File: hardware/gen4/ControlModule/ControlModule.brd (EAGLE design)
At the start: 29.9 x 59.3 mm, 39 parts, among them IC1 XMEGA16A4A

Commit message: pdi fix
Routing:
- net DATA: track 0.00 -> 37.0 mm, vias 0 -> 1
- net GND: track 111.1 -> 108.1 mm
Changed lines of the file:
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@@
 <wire x1="41.43375" y1="9.2075" x2="42.4815" y2="9.2075" width="0.254" layer="1"/>
 <wire x1="42.4815" y1="9.2075" x2="42.545" y2="9.271" width="0.254" layer="1"/>
-<wire x1="42.46" y1="26.06" x2="43.79" y2="26.06" width="0.1524" layer="1"/>
-<wire x1="43.79" y1="26.06" x2="45.24375" y2="24.685625" width="0.1524" layer="1"/>
-<wire x1="45.24375" y1="24.685625" x2="45.24375" y2="20.955" width="0.1524" layer="1"/>
+<wire x1="42.46" y1="26.06" x2="43.31375" y2="26.06" width="0.1524" layer="1"/>
+<wire x1="43.31375" y1="26.06" x2="45.24375" y2="24.28875" width="0.1524" layer="1"/>
+<wire x1="45.24375" y1="24.28875" x2="45.24375" y2="20.955" width="0.1524" layer="1"/>
 <wire x1="45.24375" y1="20.955" x2="44.45" y2="20.16125" width="0.1524" layer="1"/>
 <wire x1="44.45" y1="20.16125" x2="44.45" y2="19.3675" width="0.1524" layer="1"/>
@@
 <contactref element="S3" pad="2"/>
 <contactref element="S1" pad="2"/>
-<wire x1="61.595" y1="22.225" x2="59.84875" y2="22.225" width="0.254" layer="16"/>
-<wire x1="59.84875" y1="22.225" x2="58.7375" y2="21.11375" width="0.254" layer="16"/>
+<wire x1="58.42" y1="20.955" x2="58.57875" y2="20.955" width="0.254" layer="16"/>
+<wire x1="58.57875" y1="20.955" x2="58.7375" y2="21.11375" width="0.254" layer="16"/>
 <wire x1="58.7375" y1="21.11375" x2="58.7375" y2="20.32" width="0.254" layer="16"/>
 <wire x1="58.7375" y1="19.605625" x2="58.7375" y2="20.32" width="0.254" layer="16"/>
@@
 <wire x1="38.338125" y1="21.581875" x2="39.37" y2="20.55" width="0.1778" layer="1"/>
 <contactref element="JP2" pad="6"/>
+<wire x1="59.21375" y1="30.00375" x2="54.06" y2="23.66" width="0" layer="19" extent="1-1"/>
 </signal>
 <signal name="3.3V">
@@
 <wire x1="45.86" y1="27.1275" x2="45.085" y2="26.3525" width="0.254" layer="1"/>
 <wire x1="45.085" y1="26.3525" x2="44.1325" y2="26.3525" width="0.254" layer="1"/>
-<wire x1="44.1325" y1="26.3525" x2="43.65625" y2="26.82875" width="0.254" layer="1"/>
-<wire x1="43.65625" y1="26.82875" x2="43.65625" y2="27.305" width="0.254" layer="1"/>
+<wire x1="44.1325" y1="26.3525" x2="43.815" y2="26.749375" width="0.254" layer="1"/>
+<wire x1="43.815" y1="26.749375" x2="43.65625" y2="27.305" width="0.254" layer="1"/>
 <wire x1="43.65625" y1="27.305" x2="43.4975" y2="27.46375" width="0.254" layer="1"/>
 <wire x1="43.4975" y1="27.46375" x2="40.9575" y2="27.46375" width="0.254" layer="1"/>
@@
 <contactref element="IC1" pad="34"/>
 <contactref element="JP2" pad="1"/>
-<wire x1="42.46" y1="26.86" x2="60.325" y2="26.035" width="0" layer="19" extent="1-1"/>
+<wire x1="42.46" y1="26.86" x2="43.3075" y2="26.86" width="0.1778" layer="1"/>
+<wire x1="43.3075" y1="26.86" x2="43.33875" y2="26.82875" width="0.1778" layer="1"/>
+<wire x1="43.33875" y1="26.82875" x2="43.33875" y2="26.51125" width="0.1778" layer="1"/>
+<wire x1="43.33875" y1="26.51125" x2="44.60875" y2="25.24125" width="0.1778" layer="1"/>
+<wire x1="44.60875" y1="25.24125" x2="47.46625" y2="25.24125" width="0.1778" layer="1"/>
+<wire x1="47.46625" y1="25.24125" x2="48.021875" y2="24.685625" width="0.1778" layer="1"/>
+<wire x1="48.021875" y1="24.685625" x2="49.768125" y2="24.685625" width="0.1778" layer="1"/>
+<wire x1="49.768125" y1="24.685625" x2="50.244375" y2="24.209375" width="0.1778" layer="1"/>
+<wire x1="50.244375" y1="24.209375" x2="50.244375" y2="19.05" width="0.1778" layer="1"/>
+<via x="50.244375" y="19.05" extent="1-16" drill="0.6"/>
+<wire x1="50.244375" y1="19.05" x2="50.561875" y2="19.05" width="0.1778" layer="16"/>
+<wire x1="50.561875" y1="19.05" x2="51.038125" y2="19.52625" width="0.1778" layer="16"/>
+<wire x1="51.038125" y1="19.52625" x2="51.038125" y2="21.2725" width="0.1778" layer="16"/>
+<wire x1="51.038125" y1="21.2725" x2="51.355625" y2="21.59" width="0.1778" layer="16"/>
+<wire x1="51.355625" y1="21.59" x2="51.831875" y2="21.59" width="0.1778" layer="16"/>
+<wire x1="51.831875" y1="21.59" x2="52.22875" y2="21.193125" width="0.1778" layer="16"/>
+<wire x1="52.22875" y1="21.193125" x2="52.22875" y2="19.446875" width="0.1778" layer="16"/>
+<wire x1="52.22875" y1="19.446875" x2="53.18125" y2="18.494375" width="0.1778" layer="16"/>
+<wire x1="53.18125" y1="18.494375" x2="58.181875" y2="18.494375" width="0.1778" layer="16"/>
+<wire x1="58.181875" y1="18.494375" x2="59.3725" y2="19.685" width="0.1778" layer="16"/>
+<wire x1="59.3725" y1="19.685" x2="59.3725" y2="19.84375" width="0.1778" layer="16"/>
+<wire x1="59.3725" y1="19.84375" x2="59.293125" y2="20.79625" width="0.1778" layer="16"/>
+<wire x1="59.293125" y1="20.79625" x2="59.293125" y2="21.74875" width="0.1778" layer="16"/>
+<wire x1="59.293125" y1="21.74875" x2="59.769375" y2="22.225" width="0.1778" layer="16"/>
+<wire x1="59.769375" y1="22.225" x2="61.43625" y2="22.225" width="0.1778" layer="16"/>
+<wire x1="61.43625" y1="22.225" x2="61.595" y2="22.38375" width="0.1778" layer="16"/>
+<wire x1="61.595" y1="22.38375" x2="61.595" y2="24.765" width="0.1778" layer="16"/>
+<wire x1="61.595" y1="24.765" x2="60.325" y2="26.035" width="0.1778" layer="16"/>
 </signal>
 <signal name="SS_4">

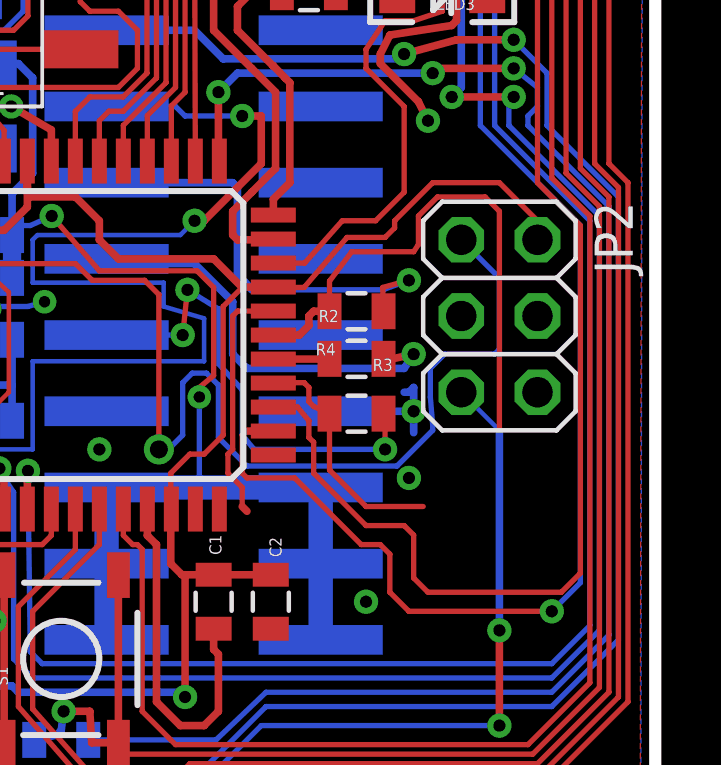
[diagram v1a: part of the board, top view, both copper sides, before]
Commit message: redid debug connector on comms, but clearance checks havent been done
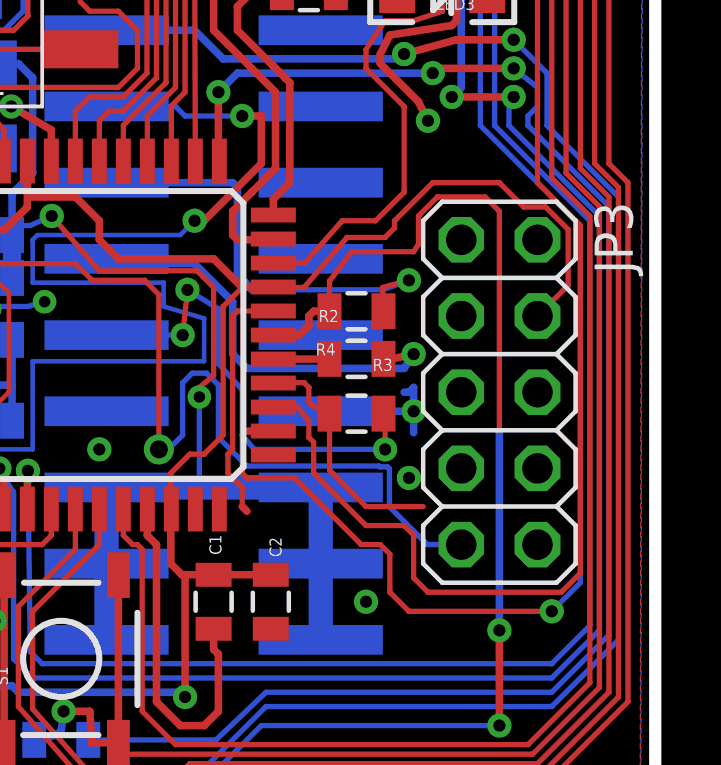
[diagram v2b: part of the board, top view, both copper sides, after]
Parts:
- removed JP2: (no value), pinhead:2X03
- added JP3: DEBUG, pinhead:2X05
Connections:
- net N$1 renamed AVCC
- removed net INT: IC1.12
- removed net SCL: IC1.11
- removed net SDA: IC1.10
- net 3.3V: now also JP3.4; no longer JP2.2
- net DATA: now also JP3.9; no longer JP2.1
- net GND: now also JP3.10; no longer JP2.6
- net RESET: now also JP3.6; no longer JP2.5
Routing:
- net DATA: track 37.0 -> 30.5 mm
- net 3.3V: track 163.0 -> 166.8 mm
- net RESET: track 58.1 -> 56.3 mm
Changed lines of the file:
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@@
 <?xml version="1.0" encoding="utf-8"?>
 <!DOCTYPE eagle SYSTEM "eagle.dtd">
-<eagle version="7.2.0">
+<eagle version="7.5.0">
 <drawing>
 <settings>
@@
 <setting verticaltext="up"/>
 </settings>
-<grid distance="25" unitdist="mil" unit="mil" style="lines" multiple="1" display="yes" altdistance="3.125" altunitdist="mil" altunit="mil"/>
+<grid distance="0.000123031496" unitdist="mil" unit="mil" style="lines" multiple="1" display="yes" altdistance="0.000123031496" altunitdist="mil" altunit="mil"/>
 <layers>
 <layer number="1" name="Top" color="4" fill="1" visible="yes" active="yes"/>
@@
 <attribute name="PROD_ID" value="SWCH-08247" x="46.99" y="12.065" size="1.778" layer="27" rot="R90" display="off"/>
 </element>
-<element name="JP2" library="pinhead" package="2X03" value="" x="61.595" y="23.495" rot="R270"/>
+<element name="JP3" library="pinhead" package="2X05" value="DEBUG" x="61.595" y="20.955" rot="R270"/>
 </elements>
 <signals>
@@
 <wire x1="51.435" y1="7.62" x2="40.64" y2="7.62" width="0.1778" layer="16"/>
 <wire x1="40.64" y1="7.62" x2="40.005" y2="8.255" width="0.1778" layer="16"/>
-<contactref element="JP2" pad="5"/>
-<wire x1="61.595" y1="19.685" x2="60.325" y2="20.955" width="0.1524" layer="16"/>
+<contactref element="JP3" pad="6"/>
+<wire x1="61.595" y1="19.685" x2="62.865" y2="20.955" width="0" layer="19" extent="16-16"/>
 </signal>
 <signal name="GND">
@@
 <wire x1="38.338125" y1="24.844375" x2="38.338125" y2="21.581875" width="0.1778" layer="1"/>
 <wire x1="38.338125" y1="21.581875" x2="39.37" y2="20.55" width="0.1778" layer="1"/>
-<contactref element="JP2" pad="6"/>
-<wire x1="59.21375" y1="30.00375" x2="54.06" y2="23.66" width="0" layer="19" extent="1-1"/>
+<contactref element="JP3" pad="10"/>
+<wire x1="55.6387" y1="20.32" x2="52.705" y2="19.05" width="0" layer="19" extent="1-16"/>
 </signal>
 <signal name="3.3V">
@@
 <wire x1="40.9575" y1="27.46375" x2="40.64" y2="27.78125" width="0.254" layer="1"/>
 <via x="40.64" y="27.78125" extent="1-16" drill="0.4064" diameter="0.254"/>
-<wire x1="62.865" y1="26.67" x2="61.595" y2="27.94" width="0.1778" layer="1"/>
 <wire x1="61.595" y1="27.94" x2="59.3725" y2="27.94" width="0.1778" layer="1"/>
 <wire x1="59.3725" y1="27.94" x2="58.1025" y2="26.67" width="0.1778" layer="1"/>
@@
 <wire x1="38.1" y1="34.925" x2="39.575" y2="34.925" width="0.1524" layer="16"/>
 <wire x1="39.575" y1="34.925" x2="39.61" y2="34.89" width="0.254" layer="16"/>
-<contactref element="JP2" pad="2"/>
-<wire x1="62.865" y1="26.67" x2="62.865" y2="26.035" width="0.1524" layer="1"/>
+<contactref element="JP3" pad="4"/>
+<wire x1="61.595" y1="27.94" x2="62.40429375" y2="27.13070625" width="0.1778" layer="1"/>
+<wire x1="62.40429375" y1="27.13070625" x2="63.135603125" y2="27.13070625" width="0.1778" layer="1"/>
+<wire x1="63.135603125" y1="27.13070625" x2="63.88685" y2="26.379459375" width="0.1778" layer="1"/>
+<wire x1="63.88685" y1="26.379459375" x2="63.88685" y2="24.51685" width="0.1778" layer="1"/>
+<wire x1="63.88685" y1="24.51685" x2="62.865" y2="23.495" width="0.1778" layer="1"/>
 </signal>
-<signal name="N$1">
+<signal name="AVCC">
 <contactref element="IC1" pad="39"/>
 <contactref element="R1" pad="1"/>
@@
 <wire x1="46.99" y1="9.68375" x2="47.069375" y2="10.31875" width="0.254" layer="16"/>
 </signal>
-<signal name="SCL">
-<contactref element="IC1" pad="11"/>
-</signal>
-<signal name="SDA">
-<contactref element="IC1" pad="10"/>
-</signal>
 <signal name="12V">
 <contactref element="R8" pad="2"/>
@@
 <wire x1="58.42" y1="43.18" x2="55.6387" y2="43.18" width="0.254" layer="16"/>
 </signal>
-<signal name="INT">
-<contactref element="IC1" pad="12"/>
-</signal>
 <signal name="GLED1">
 <contactref element="R13" pad="2"/>
@@
 <signal name="DATA">
 <contactref element="IC1" pad="34"/>
-<contactref element="JP2" pad="1"/>
 <wire x1="42.46" y1="26.86" x2="43.3075" y2="26.86" width="0.1778" layer="1"/>
 <wire x1="43.3075" y1="26.86" x2="43.33875" y2="26.82875" width="0.1778" layer="1"/>
@@
 <wire x1="52.22875" y1="21.193125" x2="52.22875" y2="19.446875" width="0.1778" layer="16"/>
 <wire x1="52.22875" y1="19.446875" x2="53.18125" y2="18.494375" width="0.1778" layer="16"/>
-<wire x1="53.18125" y1="18.494375" x2="58.181875" y2="18.494375" width="0.1778" layer="16"/>
-<wire x1="58.181875" y1="18.494375" x2="59.3725" y2="19.685" width="0.1778" layer="16"/>
-<wire x1="59.3725" y1="19.685" x2="59.3725" y2="19.84375" width="0.1778" layer="16"/>
-<wire x1="59.3725" y1="19.84375" x2="59.293125" y2="20.79625" width="0.1778" layer="16"/>
-<wire x1="59.293125" y1="20.79625" x2="59.293125" y2="21.74875" width="0.1778" layer="16"/>
-<wire x1="59.293125" y1="21.74875" x2="59.769375" y2="22.225" width="0.1778" layer="16"/>
-<wire x1="59.769375" y1="22.225" x2="61.43625" y2="22.225" width="0.1778" layer="16"/>
-<wire x1="61.43625" y1="22.225" x2="61.595" y2="22.38375" width="0.1778" layer="16"/>
-<wire x1="61.595" y1="22.38375" x2="61.595" y2="24.765" width="0.1778" layer="16"/>
-<wire x1="61.595" y1="24.765" x2="60.325" y2="26.035" width="0.1778" layer="16"/>
+<wire x1="53.18125" y1="18.494375" x2="57.582759375" y2="18.494375" width="0.1778" layer="16"/>
+<contactref element="JP3" pad="9"/>
+<wire x1="57.582759375" y1="18.494375" x2="57.610390625" y2="18.46674375" width="0.1778" layer="16"/>
+<wire x1="57.610390625" y1="18.46674375" x2="57.862190625" y2="18.46674375" width="0.1778" layer="16"/>
+<wire x1="57.862190625" y1="18.46674375" x2="57.9305875" y2="18.398346875" width="0.1778" layer="16"/>
+<wire x1="57.9305875" y1="18.398346875" x2="57.9305875" y2="17.13545625" width="0.1778" layer="16"/>
+<wire x1="57.9305875" y1="17.13545625" x2="59.188384375" y2="15.877659375" width="0.1778" layer="16"/>
+<wire x1="59.188384375" y1="15.877659375" x2="60.322340625" y2="15.877659375" width="0.1778" layer="16"/>
+<wire x1="60.322340625" y1="15.877659375" x2="60.325" y2="15.875" width="0.1778" layer="16"/>
 </signal>
 <signal name="SS_4">

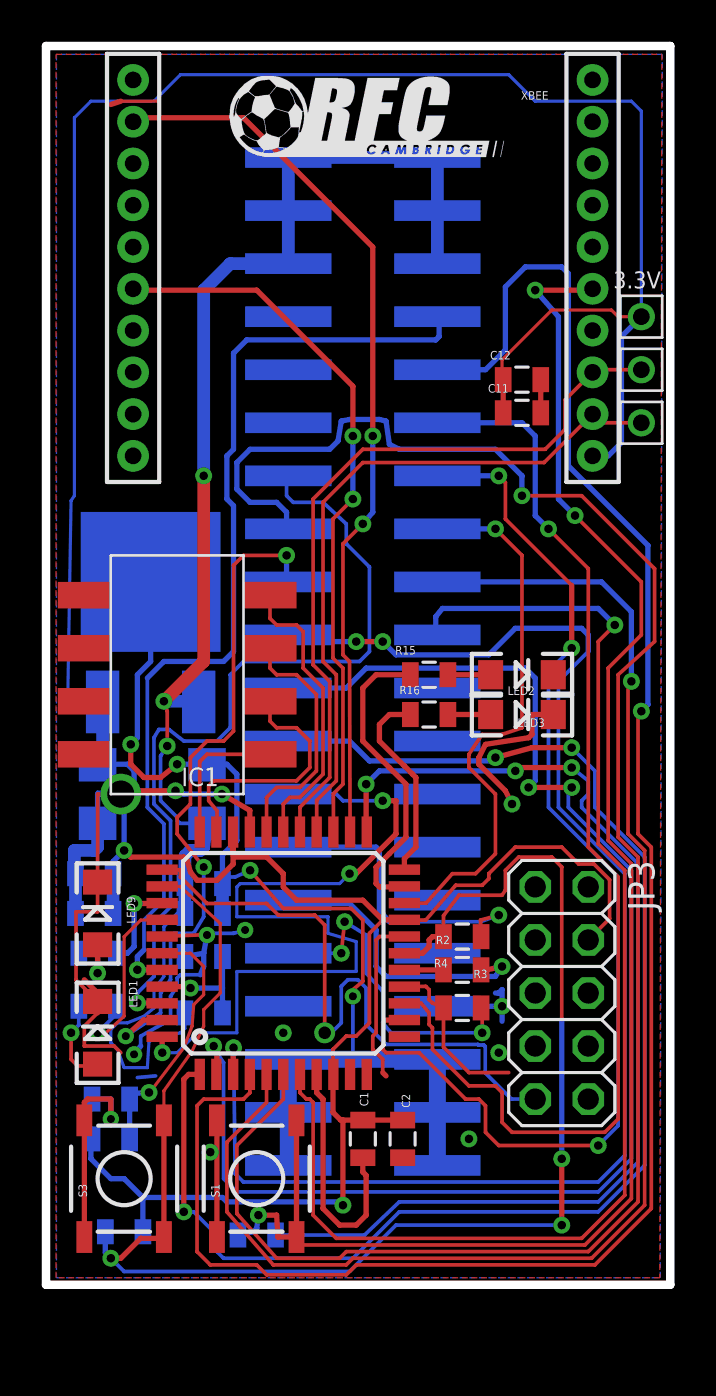
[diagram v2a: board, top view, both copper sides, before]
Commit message: comms board conditionally done - still needs work
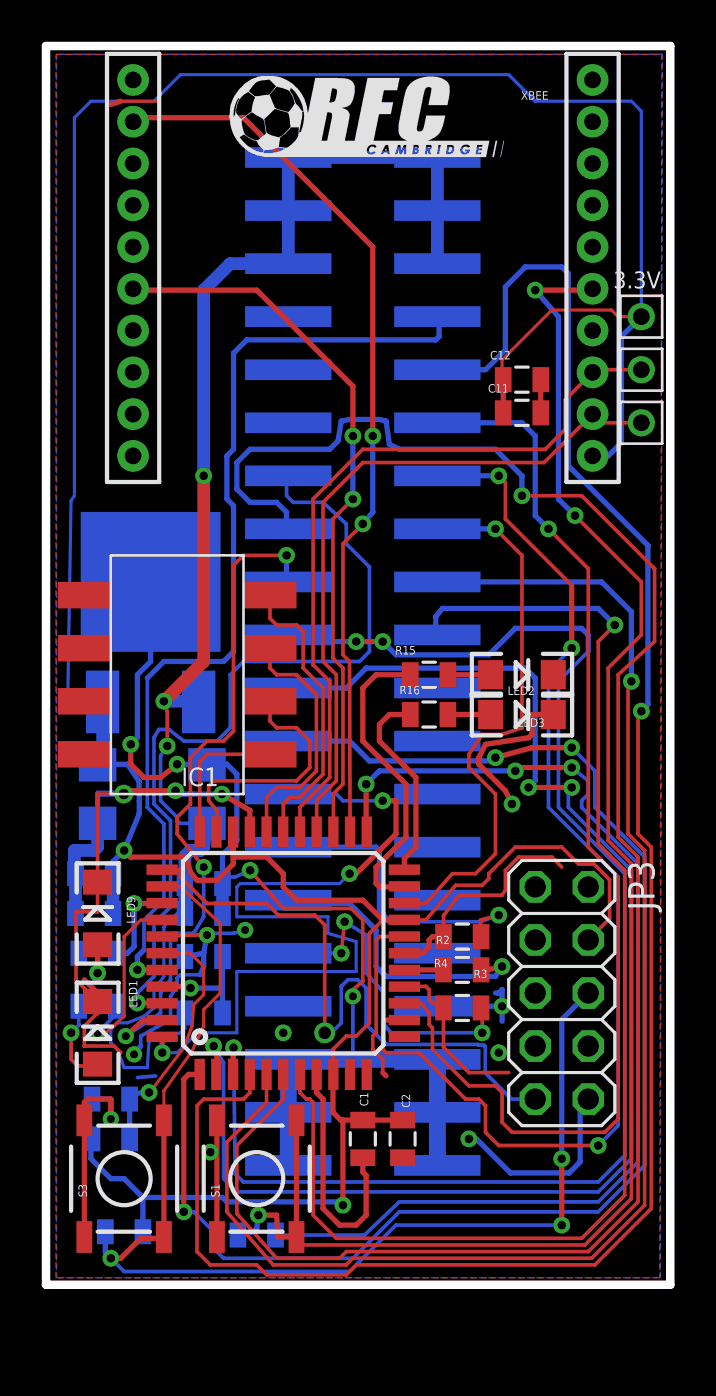
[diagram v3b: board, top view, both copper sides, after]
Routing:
- net GND: track 108.1 -> 117.7 mm
- net SCK: track 18.4 -> 11.1 mm
- net RESET: track 56.3 -> 58.1 mm
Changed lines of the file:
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@@
 <?xml version="1.0" encoding="utf-8"?>
 <!DOCTYPE eagle SYSTEM "eagle.dtd">
-<eagle version="7.5.0">
+<eagle version="7.2.0">
 <drawing>
 <settings>
@@
 <wire x1="59.53125" y1="27.46375" x2="61.11875" y2="27.46375" width="0.1778" layer="1"/>
 <wire x1="61.11875" y1="27.46375" x2="61.595" y2="26.9875" width="0.1778" layer="1"/>
-<wire x1="61.595" y1="26.9875" x2="61.595" y2="19.685" width="0.1778" layer="1"/>
 </signal>
 <signal name="TX">
@@
 <wire x1="40.64" y1="7.62" x2="40.005" y2="8.255" width="0.1778" layer="16"/>
 <contactref element="JP3" pad="6"/>
-<wire x1="61.595" y1="19.685" x2="62.865" y2="20.955" width="0" layer="19" extent="16-16"/>
+<wire x1="61.595" y1="19.685" x2="62.865" y2="20.955" width="0.254" layer="16"/>
 </signal>
 <signal name="GND">
@@
 <wire x1="43.100625" y1="30.63875" x2="40.9575" y2="30.63875" width="0.254" layer="1"/>
 <wire x1="40.9575" y1="30.63875" x2="40.79875" y2="30.48" width="0.254" layer="1"/>
-<wire x1="40.79875" y1="30.48" x2="40.48125" y2="30.48" width="0.254" layer="1"/>
-<wire x1="40.48125" y1="30.48" x2="39.37" y2="30.48" width="0.254" layer="16"/>
+<wire x1="40.79875" y1="30.48" x2="40.621853125" y2="30.48" width="0.254" layer="1"/>
+<wire x1="40.621853125" y1="30.48" x2="39.37" y2="30.48" width="0.254" layer="16"/>
 <wire x1="39.37" y1="30.48" x2="39.37" y2="29.08" width="0.254" layer="16"/>
 <wire x1="39.105" y1="15.875" x2="40.005" y2="15.875" width="0.254" layer="16"/>
@@
 <wire x1="39.37" y1="27.78125" x2="39.37" y2="30.559375" width="0.1778" layer="16"/>
 <wire x1="39.37" y1="30.559375" x2="40.48125" y2="30.559375" width="0.1778" layer="16"/>
-<wire x1="40.48125" y1="30.559375" x2="40.48125" y2="30.48" width="0.1778" layer="16"/>
-<via x="40.48125" y="30.48" extent="1-16" drill="1.3" diameter="0.254" shape="octagon"/>
-<wire x1="40.48125" y1="30.48" x2="39.37" y2="30.48" width="0.1778" layer="1"/>
+<wire x1="40.48125" y1="30.559375" x2="40.621853125" y2="30.48" width="0.1778" layer="16"/>
+<via x="40.621853125" y="30.48" extent="1-16" drill="0.5"/>
+<wire x1="40.621853125" y1="30.48" x2="39.37" y2="30.48" width="0.1778" layer="1"/>
 <wire x1="39.37" y1="30.48" x2="39.37" y2="24.844375" width="0.1778" layer="1"/>
 <wire x1="39.37" y1="24.844375" x2="38.338125" y2="24.844375" width="0.1778" layer="1"/>
@@
 <wire x1="38.338125" y1="21.581875" x2="39.37" y2="20.55" width="0.1778" layer="1"/>
 <contactref element="JP3" pad="10"/>
-<wire x1="55.6387" y1="20.32" x2="52.705" y2="19.05" width="0" layer="19" extent="1-16"/>
+<wire x1="57.15" y1="13.97" x2="57.5072625" y2="13.97" width="0.254" layer="16"/>
+<wire x1="57.5072625" y1="13.97" x2="59.139884375" y2="12.337378125" width="0.254" layer="16"/>
+<wire x1="59.139884375" y1="12.337378125" x2="61.94595" y2="12.337378125" width="0.254" layer="16"/>
+<wire x1="61.94595" y1="12.337378125" x2="62.47425625" y2="12.865684375" width="0.254" layer="16"/>
+<wire x1="62.47425625" y1="12.865684375" x2="62.47425625" y2="15.48425625" width="0.254" layer="16"/>
+<wire x1="62.47425625" y1="15.48425625" x2="62.865" y2="15.875" width="0.254" layer="16"/>
 </signal>
 <signal name="3.3V">
@@
 <wire x1="40.11125" y1="26.67" x2="40.11125" y2="27.2525" width="0.254" layer="16"/>
 <wire x1="40.11125" y1="27.2525" x2="40.64" y2="27.78125" width="0.254" layer="16"/>
-<wire x1="40.64" y1="27.78125" x2="40.64" y2="29.68625" width="0.254" layer="16"/>
-<wire x1="40.64" y1="29.68625" x2="41.11625" y2="30.1625" width="0.254" layer="16"/>
-<wire x1="41.11625" y1="30.1625" x2="41.11625" y2="31.59125" width="0.254" layer="16"/>
-<wire x1="41.11625" y1="31.59125" x2="40.79875" y2="31.90875" width="0.254" layer="16"/>
+<wire x1="40.64" y1="27.78125" x2="41.3639" y2="29.539278125" width="0.254" layer="16"/>
+<wire x1="41.3639" y1="29.539278125" x2="41.366621875" y2="30.15705625" width="0.254" layer="16"/>
+<wire x1="41.366621875" y1="30.15705625" x2="41.35210625" y2="31.096828125" width="0.254" layer="16"/>
+<wire x1="41.35210625" y1="31.096828125" x2="40.79875" y2="31.90875" width="0.254" layer="16"/>
 <wire x1="40.79875" y1="31.90875" x2="39.39875" y2="31.90875" width="0.254" layer="16"/>
 <wire x1="39.39875" y1="31.90875" x2="39.37" y2="31.88" width="0.254" layer="16"/>
